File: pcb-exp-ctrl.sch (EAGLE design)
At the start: 14 parts, among them IC1 SAA1064, IC2 TINY13-20PU, T1 BC547, T2 BC547

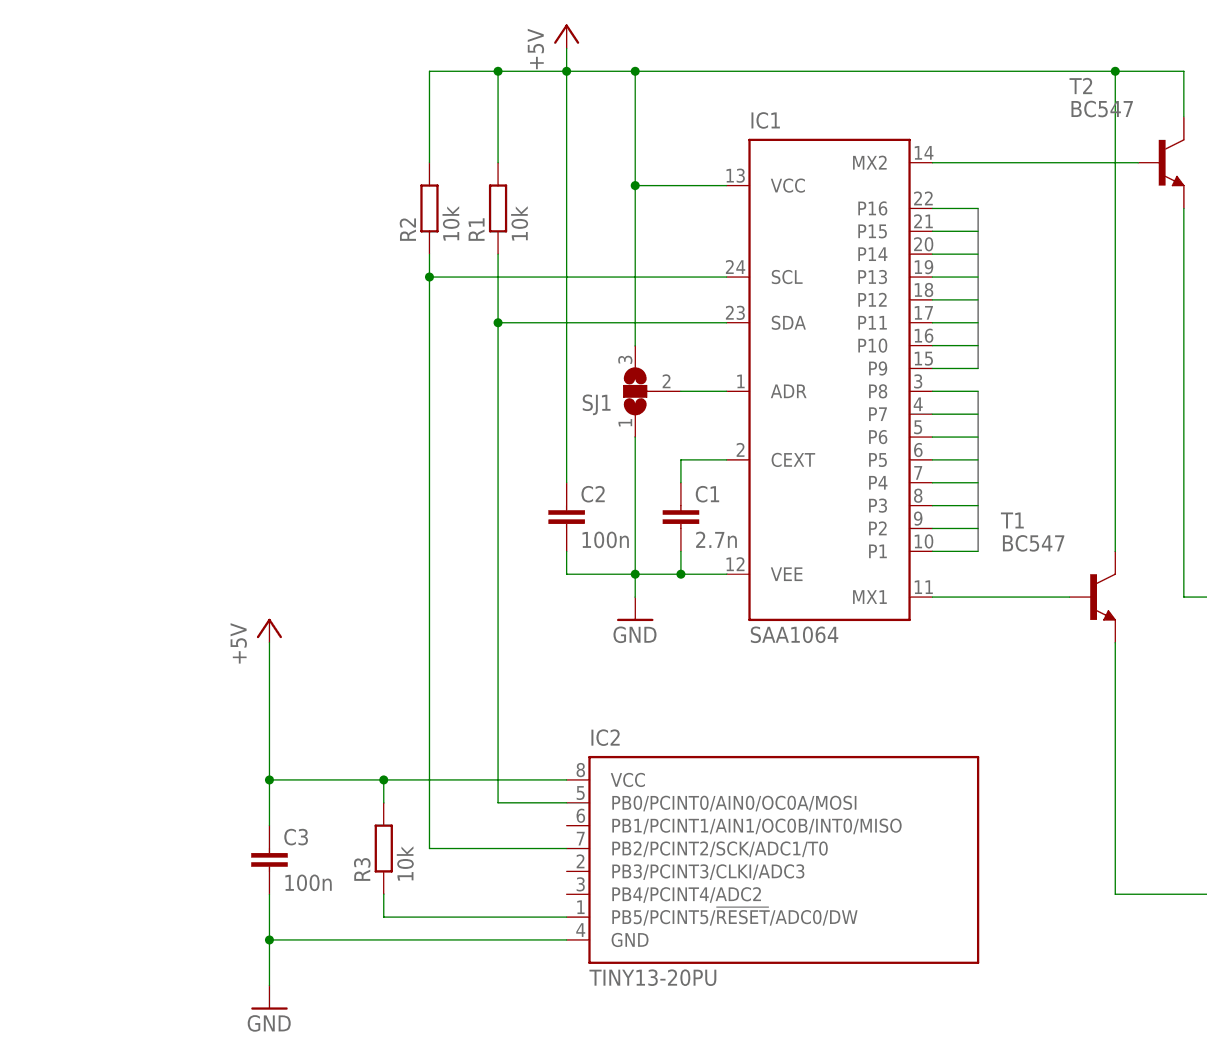
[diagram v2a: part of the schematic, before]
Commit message: add programmer header and connect to uC
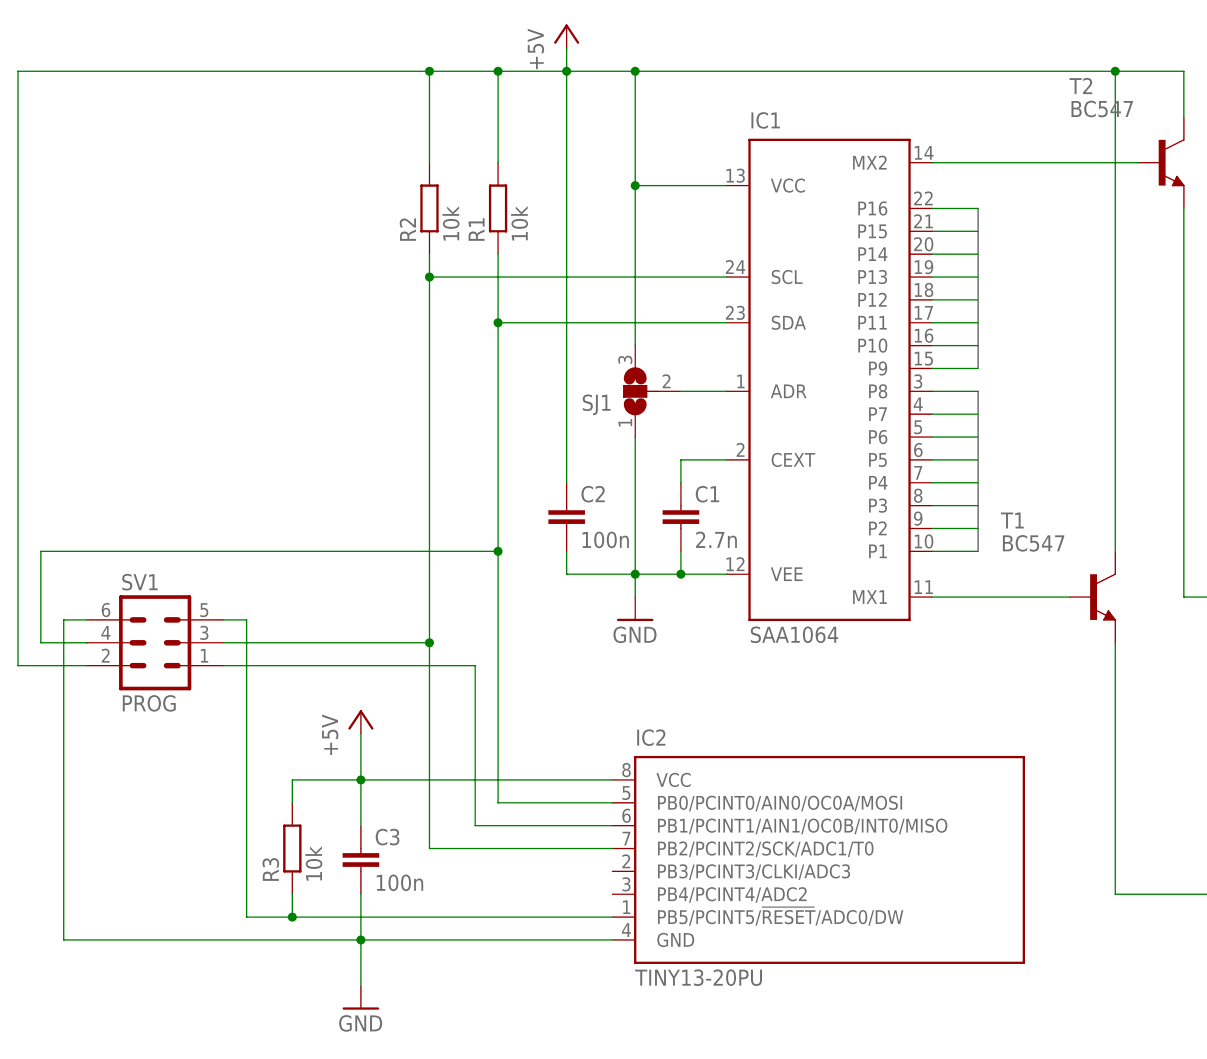
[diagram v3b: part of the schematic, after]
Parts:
- added SV1: PROG, con-ml:ML6
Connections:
- removed net N$1: IC1.SCL, IC2.PB2/PCINT2/SCK/ADC1/T0, R2.1
- removed net N$11: IC2.PB5/PCINT5/!RESET!/ADC0/DW, R3.1
- removed net N$3: IC1.SDA, IC2.PB0/PCINT0/AIN0/OC0A/MOSI, R1.1
- new net MISO: IC2.PB1/PCINT1/AIN1/OC0B/INT0/MISO, SV1.1
- new net MOSI: IC1.SDA, IC2.PB0/PCINT0/AIN0/OC0A/MOSI, R1.1, SV1.4
- new net SCK: IC1.SCL, IC2.PB2/PCINT2/SCK/ADC1/T0, R2.1, SV1.3
- new net _RESET: IC2.PB5/PCINT5/!RESET!/ADC0/DW, R3.1, SV1.5
- net +5V: now also SV1.2
- net GND: now also SV1.6
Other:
- moved on the sheet: C3, IC2, R3
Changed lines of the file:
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@@
 <part name="C3" library="rcl" deviceset="C-EU" device="025-025X050" value="100n"/>
 <part name="R3" library="rcl" deviceset="R-EU_" device="0204/7" value="10k"/>
+<part name="SV1" library="con-ml" deviceset="ML6" device="" value="PROG"/>
 </parts>
 <sheets>
@@
 <attribute name="VALUE" x="12.7" y="35.56" size="1.778" layer="96"/>
 </instance>
-<instance part="IC2" gate="G$1" x="12.7" y="7.62"/>
+<instance part="IC2" gate="G$1" x="17.78" y="7.62"/>
 <instance part="LED1" gate="G$1" x="88.9" y="81.28"/>
 <instance part="LED2" gate="G$1" x="88.9" y="55.88"/>
 <instance part="LED3" gate="G$1" x="88.9" y="22.86"/>
-<instance part="GND1" gate="1" x="-40.64" y="-5.08"/>
+<instance part="GND1" gate="1" x="-30.48" y="-5.08"/>
 <instance part="GND2" gate="1" x="0" y="38.1"/>
 <instance part="P+1" gate="1" x="-7.62" y="104.14"/>
-<instance part="P+2" gate="1" x="-40.64" y="38.1"/>
+<instance part="P+2" gate="1" x="-30.48" y="27.94"/>
 <instance part="SJ1" gate="G$1" x="0" y="63.5" rot="R180"/>
 <instance part="R1" gate="G$1" x="-15.24" y="83.82" rot="R90"/>
@@
 <instance part="T1" gate="G$1" x="50.8" y="40.64"/>
 <instance part="C2" gate="G$1" x="-7.62" y="50.8"/>
-<instance part="C3" gate="G$1" x="-40.64" y="12.7"/>
-<instance part="R3" gate="G$1" x="-27.94" y="12.7" rot="R90"/>
+<instance part="C3" gate="G$1" x="-30.48" y="12.7"/>
+<instance part="R3" gate="G$1" x="-38.1" y="12.7" rot="R90"/>
+<instance part="SV1" gate="1" x="-53.34" y="35.56"/>
 </instances>
 <busses>
@@
 </segment>
 </net>
-<net name="N$1" class="0">
+<net name="SCK" class="0">
 <segment>
 <pinref part="IC2" gate="G$1" pin="PB2/PCINT2/SCK/ADC1/T0"/>
-<wire x1="-7.62" y1="12.7" x2="-22.86" y2="12.7" width="0.1524" layer="91"/>
-<wire x1="-22.86" y1="12.7" x2="-22.86" y2="76.2" width="0.1524" layer="91"/>
+<wire x1="-2.54" y1="12.7" x2="-22.86" y2="12.7" width="0.1524" layer="91"/>
+<wire x1="-22.86" y1="12.7" x2="-22.86" y2="35.56" width="0.1524" layer="91"/>
 <pinref part="IC1" gate="G$1" pin="SCL"/>
+<wire x1="-22.86" y1="35.56" x2="-22.86" y2="76.2" width="0.1524" layer="91"/>
 <wire x1="-22.86" y1="76.2" x2="10.16" y2="76.2" width="0.1524" layer="91"/>
 <pinref part="R2" gate="G$1" pin="1"/>
 <wire x1="-22.86" y1="78.74" x2="-22.86" y2="76.2" width="0.1524" layer="91"/>
 <junction x="-22.86" y="76.2"/>
-</segment>
-</net>
-<net name="N$3" class="0">
+<pinref part="SV1" gate="1" pin="3"/>
+<wire x1="-45.72" y1="35.56" x2="-22.86" y2="35.56" width="0.1524" layer="91"/>
+<junction x="-22.86" y="35.56"/>
+</segment>
+</net>
+<net name="MOSI" class="0">
 <segment>
 <pinref part="IC2" gate="G$1" pin="PB0/PCINT0/AIN0/OC0A/MOSI"/>
-<wire x1="-7.62" y1="17.78" x2="-15.24" y2="17.78" width="0.1524" layer="91"/>
-<wire x1="-15.24" y1="17.78" x2="-15.24" y2="71.12" width="0.1524" layer="91"/>
+<wire x1="-2.54" y1="17.78" x2="-15.24" y2="17.78" width="0.1524" layer="91"/>
+<wire x1="-15.24" y1="17.78" x2="-15.24" y2="45.72" width="0.1524" layer="91"/>
 <pinref part="IC1" gate="G$1" pin="SDA"/>
+<wire x1="-15.24" y1="45.72" x2="-15.24" y2="71.12" width="0.1524" layer="91"/>
 <wire x1="-15.24" y1="71.12" x2="10.16" y2="71.12" width="0.1524" layer="91"/>
 <pinref part="R1" gate="G$1" pin="1"/>
 <wire x1="-15.24" y1="71.12" x2="-15.24" y2="78.74" width="0.1524" layer="91"/>
 <junction x="-15.24" y="71.12"/>
+<pinref part="SV1" gate="1" pin="4"/>
+<wire x1="-60.96" y1="35.56" x2="-66.04" y2="35.56" width="0.1524" layer="91"/>
+<wire x1="-66.04" y1="35.56" x2="-66.04" y2="45.72" width="0.1524" layer="91"/>
+<wire x1="-66.04" y1="45.72" x2="-15.24" y2="45.72" width="0.1524" layer="91"/>
+<junction x="-15.24" y="45.72"/>
 </segment>
 </net>
@@
 <pinref part="GND1" gate="1" pin="GND"/>
 <pinref part="IC2" gate="G$1" pin="GND"/>
-<wire x1="-40.64" y1="-2.54" x2="-40.64" y2="2.54" width="0.1524" layer="91"/>
-<wire x1="-40.64" y1="2.54" x2="-7.62" y2="2.54" width="0.1524" layer="91"/>
+<wire x1="-30.48" y1="-2.54" x2="-30.48" y2="2.54" width="0.1524" layer="91"/>
+<wire x1="-30.48" y1="2.54" x2="-2.54" y2="2.54" width="0.1524" layer="91"/>
 <pinref part="C3" gate="G$1" pin="2"/>
-<wire x1="-40.64" y1="7.62" x2="-40.64" y2="2.54" width="0.1524" layer="91"/>
-<junction x="-40.64" y="2.54"/>
+<wire x1="-30.48" y1="7.62" x2="-30.48" y2="2.54" width="0.1524" layer="91"/>
+<junction x="-30.48" y="2.54"/>
+<pinref part="SV1" gate="1" pin="6"/>
+<wire x1="-60.96" y1="38.1" x2="-63.5" y2="38.1" width="0.1524" layer="91"/>
+<wire x1="-63.5" y1="38.1" x2="-63.5" y2="2.54" width="0.1524" layer="91"/>
+<wire x1="-63.5" y1="2.54" x2="-30.48" y2="2.54" width="0.1524" layer="91"/>
 </segment>
 <segment>
@@
 <junction x="0" y="99.06"/>
 <junction x="0" y="86.36"/>
+<pinref part="SV1" gate="1" pin="2"/>
+<wire x1="-60.96" y1="33.02" x2="-68.58" y2="33.02" width="0.1524" layer="91"/>
+<wire x1="-68.58" y1="33.02" x2="-68.58" y2="99.06" width="0.1524" layer="91"/>
+<wire x1="-68.58" y1="99.06" x2="-22.86" y2="99.06" width="0.1524" layer="91"/>
+<junction x="-22.86" y="99.06"/>
 </segment>
 <segment>
 <pinref part="P+2" gate="1" pin="+5V"/>
 <pinref part="IC2" gate="G$1" pin="VCC"/>
-<wire x1="-40.64" y1="35.56" x2="-40.64" y2="20.32" width="0.1524" layer="91"/>
-<wire x1="-40.64" y1="20.32" x2="-27.94" y2="20.32" width="0.1524" layer="91"/>
+<wire x1="-30.48" y1="25.4" x2="-30.48" y2="20.32" width="0.1524" layer="91"/>
+<wire x1="-30.48" y1="20.32" x2="-38.1" y2="20.32" width="0.1524" layer="91"/>
 <pinref part="C3" gate="G$1" pin="1"/>
-<wire x1="-27.94" y1="20.32" x2="-7.62" y2="20.32" width="0.1524" layer="91"/>
-<wire x1="-40.64" y1="15.24" x2="-40.64" y2="20.32" width="0.1524" layer="91"/>
-<junction x="-40.64" y="20.32"/>
+<wire x1="-30.48" y1="20.32" x2="-2.54" y2="20.32" width="0.1524" layer="91"/>
+<wire x1="-30.48" y1="15.24" x2="-30.48" y2="20.32" width="0.1524" layer="91"/>
+<junction x="-30.48" y="20.32"/>
 <pinref part="R3" gate="G$1" pin="2"/>
-<wire x1="-27.94" y1="17.78" x2="-27.94" y2="20.32" width="0.1524" layer="91"/>
-<junction x="-27.94" y="20.32"/>
+<wire x1="-38.1" y1="17.78" x2="-38.1" y2="20.32" width="0.1524" layer="91"/>
 </segment>
 </net>
@@
 </segment>
 </net>
-<net name="N$11" class="0">
+<net name="_RESET" class="0">
 <segment>
 <pinref part="IC2" gate="G$1" pin="PB5/PCINT5/!RESET!/ADC0/DW"/>
-<wire x1="-7.62" y1="5.08" x2="-27.94" y2="5.08" width="0.1524" layer="91"/>
+<wire x1="-2.54" y1="5.08" x2="-38.1" y2="5.08" width="0.1524" layer="91"/>
 <pinref part="R3" gate="G$1" pin="1"/>
-<wire x1="-27.94" y1="5.08" x2="-27.94" y2="7.62" width="0.1524" layer="91"/>
-</segment>
-</net>
+<wire x1="-38.1" y1="5.08" x2="-38.1" y2="7.62" width="0.1524" layer="91"/>
+<pinref part="SV1" gate="1" pin="5"/>
+<wire x1="-45.72" y1="38.1" x2="-43.18" y2="38.1" width="0.1524" layer="91"/>
+<wire x1="-43.18" y1="38.1" x2="-43.18" y2="5.08" width="0.1524" layer="91"/>
+<wire x1="-43.18" y1="5.08" x2="-38.1" y2="5.08" width="0.1524" layer="91"/>
+<junction x="-38.1" y="5.08"/>
+</segment>
+</net>
+<net name="MISO" class="0">
+<segment>
+<pinref part="IC2" gate="G$1" pin="PB1/PCINT1/AIN1/OC0B/INT0/MISO"/>
+<wire x1="-2.54" y1="15.24" x2="-17.78" y2="15.24" width="0.1524" layer="91"/>
+<wire x1="-17.78" y1="15.24" x2="-17.78" y2="33.02" width="0.1524" layer="91"/>
+<pinref part="SV1" gate="1" pin="1"/>
+<wire x1="-17.78" y1="33.02" x2="-45.72" y2="33.02" width="0.1524" layer="91"/>
+</segment>
+</net>

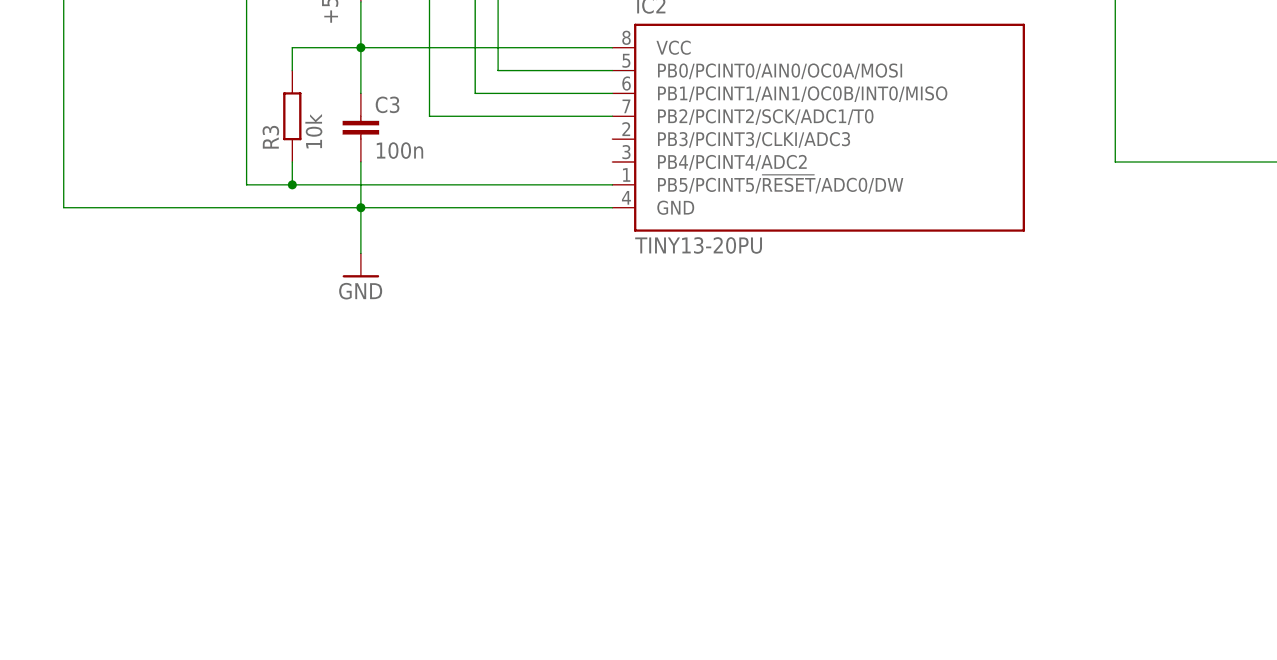
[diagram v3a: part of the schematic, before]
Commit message: drei Taster nebst integrierten LEDs hinzugefügt und teilverdrahtet
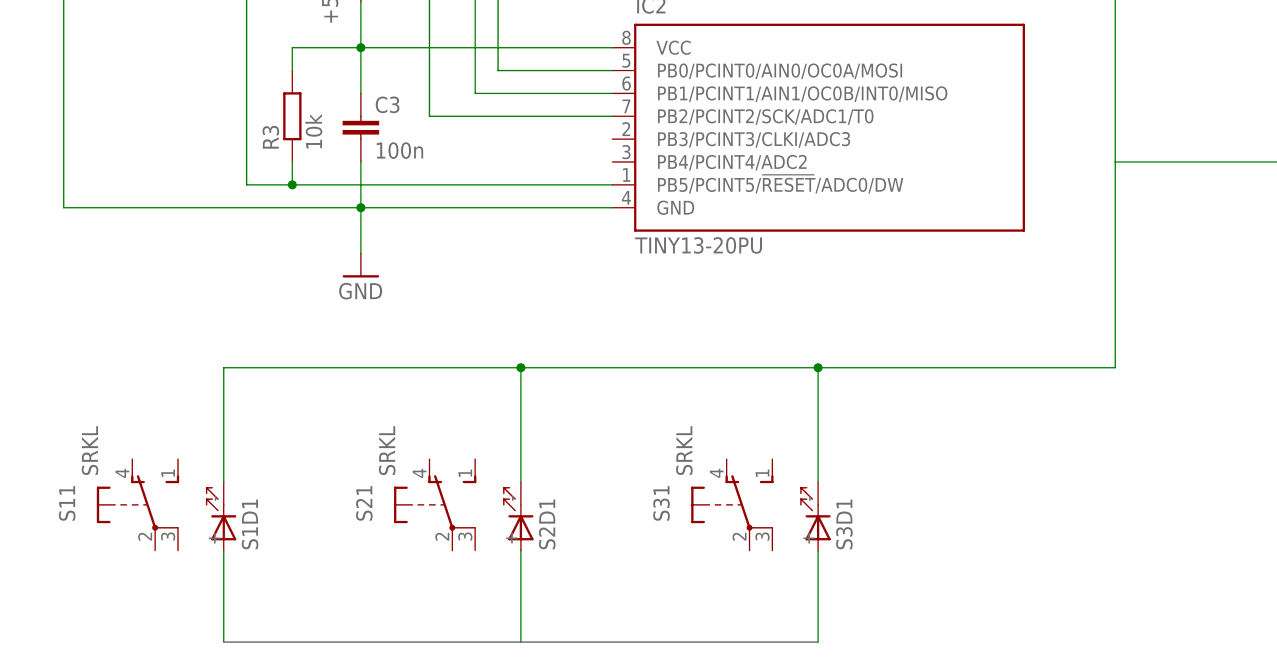
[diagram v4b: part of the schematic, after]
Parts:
- added S1, S2, S3: SRKL, switch-misc:SRKL
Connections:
- net N$7: now also S1D1.C, S2D1.C, S3D1.C
- net P10: now also S2D1.A
- net P11: now also S3D1.A
- net P9: now also S1D1.A
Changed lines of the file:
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@@
 <part name="R3" library="rcl" deviceset="R-EU_" device="0204/7" value="10k"/>
 <part name="SV1" library="con-ml" deviceset="ML6" device="" value="PROG"/>
+<part name="S1" library="switch-misc" deviceset="SRKL" device=""/>
+<part name="S2" library="switch-misc" deviceset="SRKL" device=""/>
+<part name="S3" library="switch-misc" deviceset="SRKL" device=""/>
 </parts>
 <sheets>
@@
 <instance part="R3" gate="G$1" x="-38.1" y="12.7" rot="R90"/>
 <instance part="SV1" gate="1" x="-53.34" y="35.56"/>
+<instance part="S1" gate="1" x="-53.34" y="-30.48"/>
+<instance part="S1" gate="D1" x="-45.72" y="-33.02"/>
+<instance part="S2" gate="1" x="-20.32" y="-30.48"/>
+<instance part="S2" gate="D1" x="-12.7" y="-33.02"/>
+<instance part="S3" gate="1" x="12.7" y="-30.48"/>
+<instance part="S3" gate="D1" x="20.32" y="-33.02"/>
 </instances>
 <busses>
@@
 <wire x1="73.66" y1="30.48" x2="73.66" y2="10.16" width="0.762" layer="92"/>
 <label x="71.12" y="33.02" size="1.778" layer="95"/>
+</segment>
+<segment>
+<wire x1="-45.72" y1="-45.72" x2="20.32" y2="-45.72" width="0.762" layer="92"/>
 </segment>
 </bus>
@@
 <wire x1="73.66" y1="30.48" x2="78.74" y2="30.48" width="0.1524" layer="91"/>
 </segment>
+<segment>
+<pinref part="S1" gate="D1" pin="A"/>
+<wire x1="-45.72" y1="-45.72" x2="-45.72" y2="-35.56" width="0.1524" layer="91"/>
+</segment>
 </net>
 <net name="P10" class="0">
@@
 <wire x1="73.66" y1="27.94" x2="78.74" y2="27.94" width="0.1524" layer="91"/>
 </segment>
+<segment>
+<pinref part="S2" gate="D1" pin="A"/>
+<wire x1="-12.7" y1="-45.72" x2="-12.7" y2="-35.56" width="0.1524" layer="91"/>
+</segment>
 </net>
 <net name="P11" class="0">
@@
 <pinref part="LED3" gate="G$1" pin="C"/>
 <wire x1="73.66" y1="25.4" x2="78.74" y2="25.4" width="0.1524" layer="91"/>
+</segment>
+<segment>
+<pinref part="S3" gate="D1" pin="A"/>
+<wire x1="20.32" y1="-45.72" x2="20.32" y2="-35.56" width="0.1524" layer="91"/>
 </segment>
 </net>
@@
 <junction x="111.76" y="30.48"/>
 <junction x="111.76" y="86.36"/>
-</segment>
-</net>
+<pinref part="S1" gate="D1" pin="C"/>
+<wire x1="-45.72" y1="-27.94" x2="-45.72" y2="-15.24" width="0.1524" layer="91"/>
+<wire x1="-45.72" y1="-15.24" x2="-12.7" y2="-15.24" width="0.1524" layer="91"/>
+<wire x1="-12.7" y1="-15.24" x2="20.32" y2="-15.24" width="0.1524" layer="91"/>
+<wire x1="20.32" y1="-15.24" x2="53.34" y2="-15.24" width="0.1524" layer="91"/>
+<wire x1="53.34" y1="-15.24" x2="53.34" y2="7.62" width="0.1524" layer="91"/>
+<pinref part="S2" gate="D1" pin="C"/>
+<wire x1="-12.7" y1="-27.94" x2="-12.7" y2="-15.24" width="0.1524" layer="91"/>
+<pinref part="S3" gate="D1" pin="C"/>
+<wire x1="20.32" y1="-27.94" x2="20.32" y2="-15.24" width="0.1524" layer="91"/>
+<junction x="-12.7" y="-15.24"/>
+<junction x="20.32" y="-15.24"/>
+</segment>
+</net>
